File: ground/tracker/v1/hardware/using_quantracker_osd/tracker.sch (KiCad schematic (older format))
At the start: 20 parts, among them K1 CONN_3, K2 CONN_3, M1 OSD_v2_2, P1 CONN_2, SW1 SW_PUSH

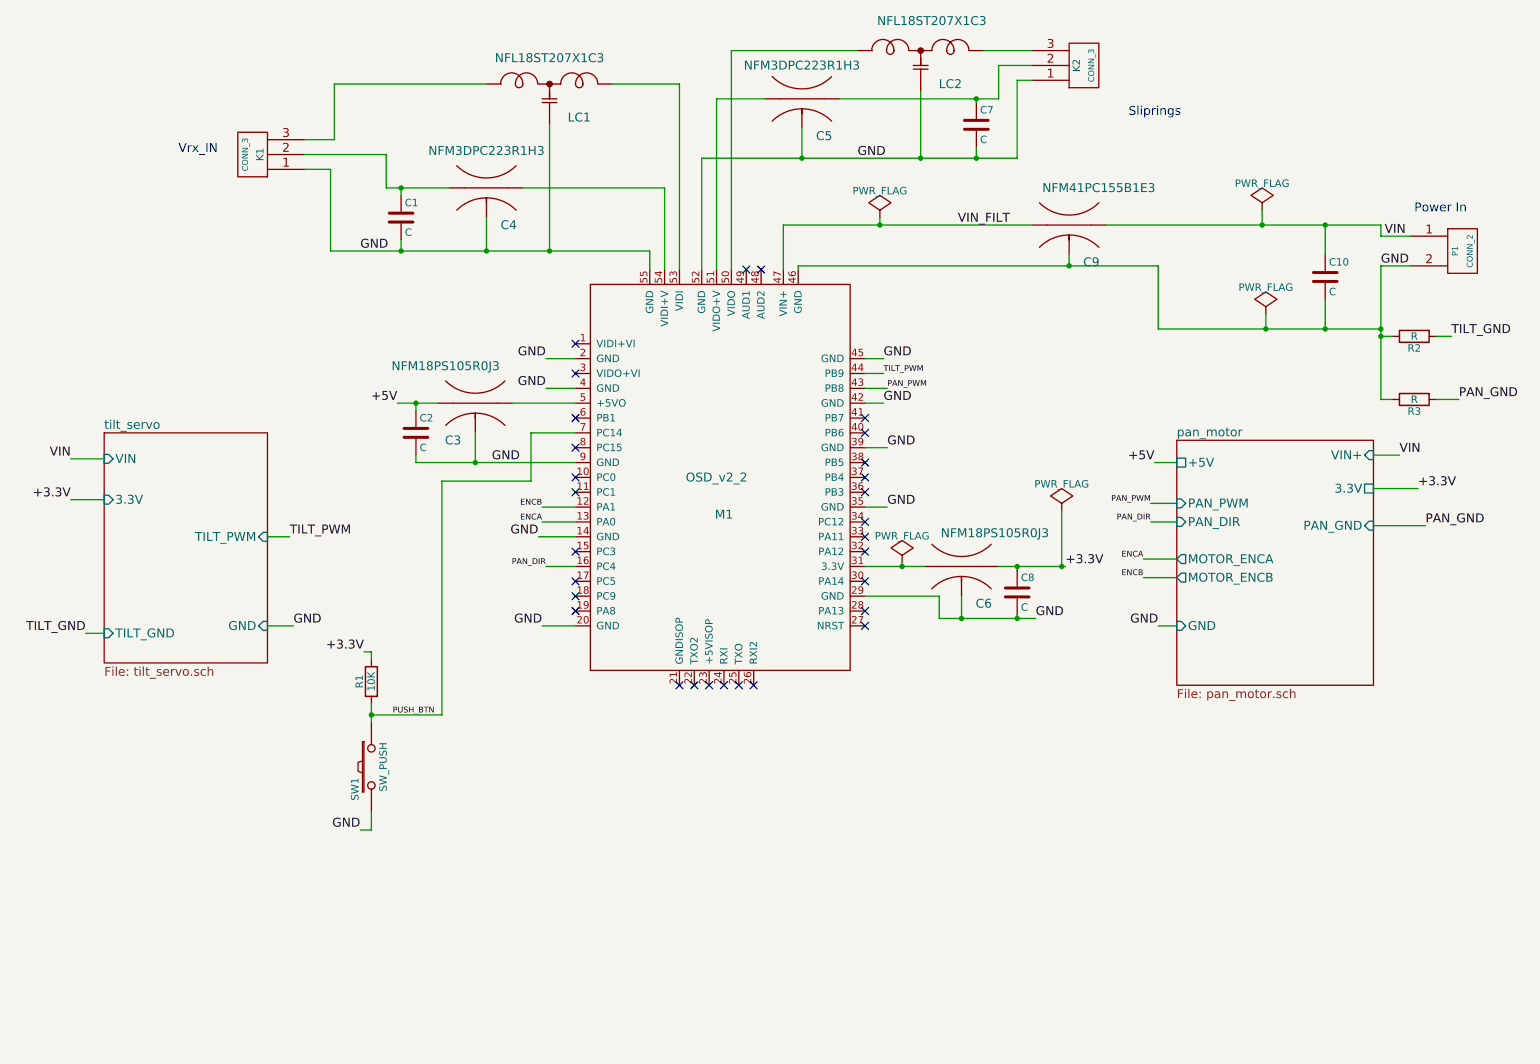
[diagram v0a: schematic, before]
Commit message: add i2c and gps connectors
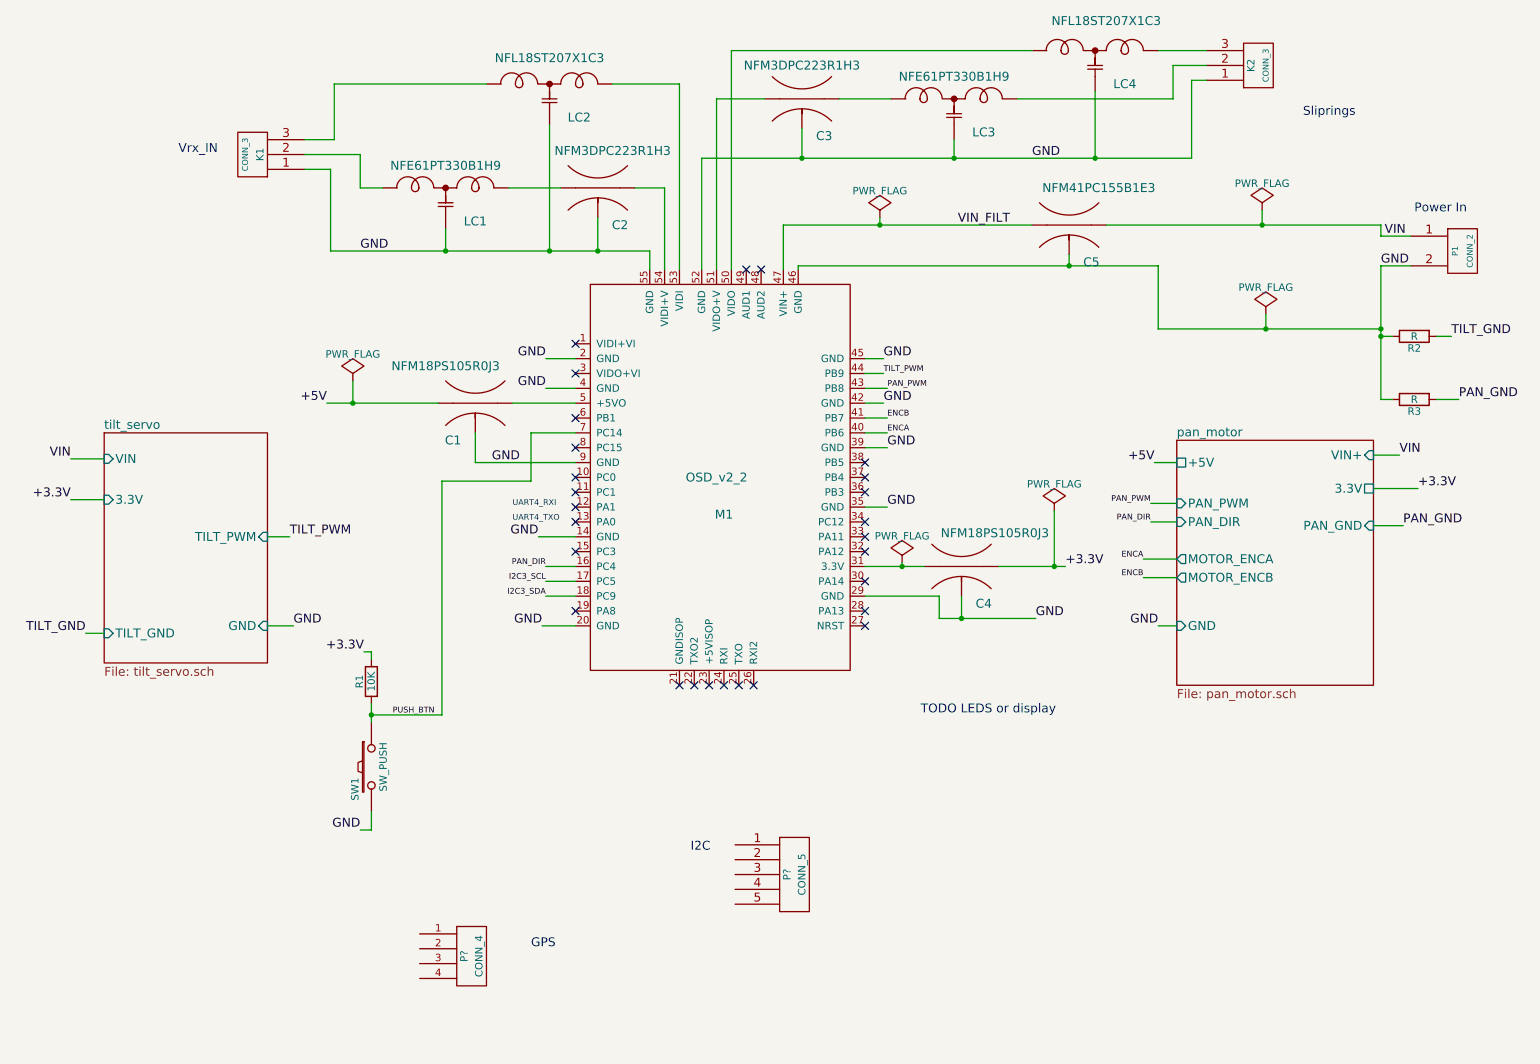
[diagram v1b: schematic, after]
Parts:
- removed C1, C10, C2, C7, C8: C, symbol C
- added LC1, LC3: NFE61PT330B1H9, symbol TLCFILT
- added P?: CONN_5, symbol CONN_5
- added P?: CONN_4, symbol CONN_4
- renumbered C3 to C1, C4 to C2, C5 to C3, C6 to C4, C9 to C5, LC1 to LC2, LC2 to LC4
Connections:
- net ENCA: now also M1.40 (PB6); no longer M1.13 (PA0)
- net ENCB: now also M1.41 (PB7); no longer M1.12 (PA1)
- net GND: now also LC1.2 (GND), LC3.2 (GND)
- net I2C3_SCL: now reaches M1.17 (PC5)
- net I2C3_SDA: now reaches M1.18 (PC9)
- net at K1.2 (PM): now also LC1.1 (Input); no longer C2.1 (IO1)
- net at K2.2 (PM): now also LC3.3 (Output); no longer C3.3 (IO2)
- new net: C2.1 (IO1), LC1.3 (Output)
- new net: C3.3 (IO2), LC3.1 (Input)
- no-connect marks 29 -> 27
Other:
- note added: "GPS"
- note added: "I2C"
- note added: "TODO LEDS or display"
- note added: "UART4_RXI"
- note added: "UART4_TXO"
- moved on the sheet: C2, K2, LC4

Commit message: move around some pin labels, preliminary still
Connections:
- net I2C3_SCL: now also M1.19 (PA8); no longer M1.17 (PC5)
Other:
- note added: "TIM11_CH1"
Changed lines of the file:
@@
 NoConn ~ 4700 3825
 NoConn ~ 4700 4225
-NoConn ~ 4700 4625
 NoConn ~ 5950 2325
 NoConn ~ 5850 2325
@@
 	1    0    0    -1
 $EndComp
-Text Label 4500 4425 2    39   ~ 0
+Text Label 4500 4625 2    39   ~ 0
 I2C3_SCL
 Text Label 4500 4525 2    39   ~ 0
 I2C3_SDA
-Wire Wire Line
-	4700 4425 4500 4425
 Wire Wire Line
 	4700 4525 4500 4525
@@
 Text Notes 5475 6250 0    60   ~ 0
 I2C
+Text Notes 6025 3050 0    39   ~ 0
+TIM11_CH1
+Wire Wire Line
+	4700 4625 4500 4625
+NoConn ~ 4700 4425
 $EndSCHEMATC

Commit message: still rearranging pinout
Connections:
- net PAN_PWM: now also M1.6 (PB1); no longer M1.43 (PB8)
- new net FrSky_PWM: M1.43 (PB8)
- no-connect marks 27 -> 26
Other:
- note added: "TIM10_CH1"
- note added: "TIM1_CH3N"
- note added: "TIM4_CH1"
- note added: "TIM4_CH2"
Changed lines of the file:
@@
 +3.3V
 Text Label 6800 3125 0    39   ~ 0
-PAN_PWM
+FrSky_PWM
 Wire Wire Line
 	6800 3125 6650 3125
@@
 NoConn ~ 6650 4625
 NoConn ~ 6650 4725
-NoConn ~ 4700 3325
 NoConn ~ 4700 3525
 NoConn ~ 4700 3725
@@
 	4700 4625 4500 4625
 NoConn ~ 4700 4425
+Text Notes 6025 3150 0    39   ~ 0
+TIM10_CH1
+Text Notes 6050 3450 0    39   ~ 0
+TIM4_CH1
+Text Notes 6075 3350 0    39   ~ 0
+TIM4_CH2
+Text Notes 5050 3350 0    39   ~ 0
+TIM1_CH3N
+Text Label 4550 3325 2    39   ~ 0
+PAN_PWM
+Wire Wire Line
+	4700 3325 4550 3325
 $EndSCHEMATC

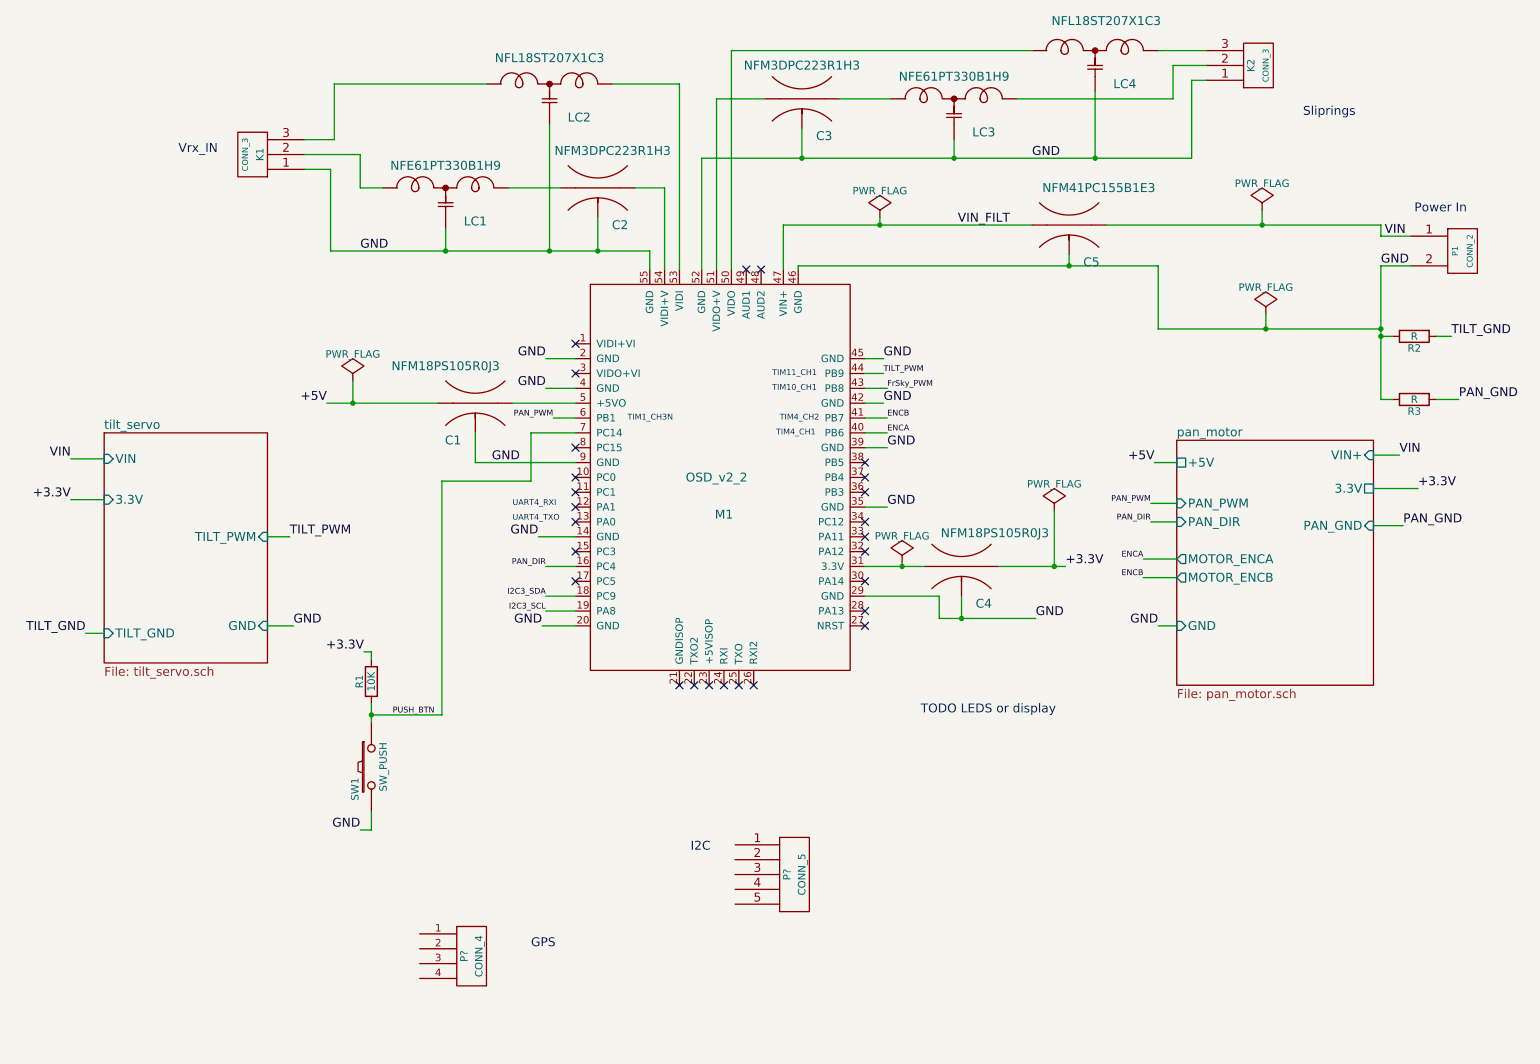
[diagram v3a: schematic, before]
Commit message: move encoder up out of pan motor schematic
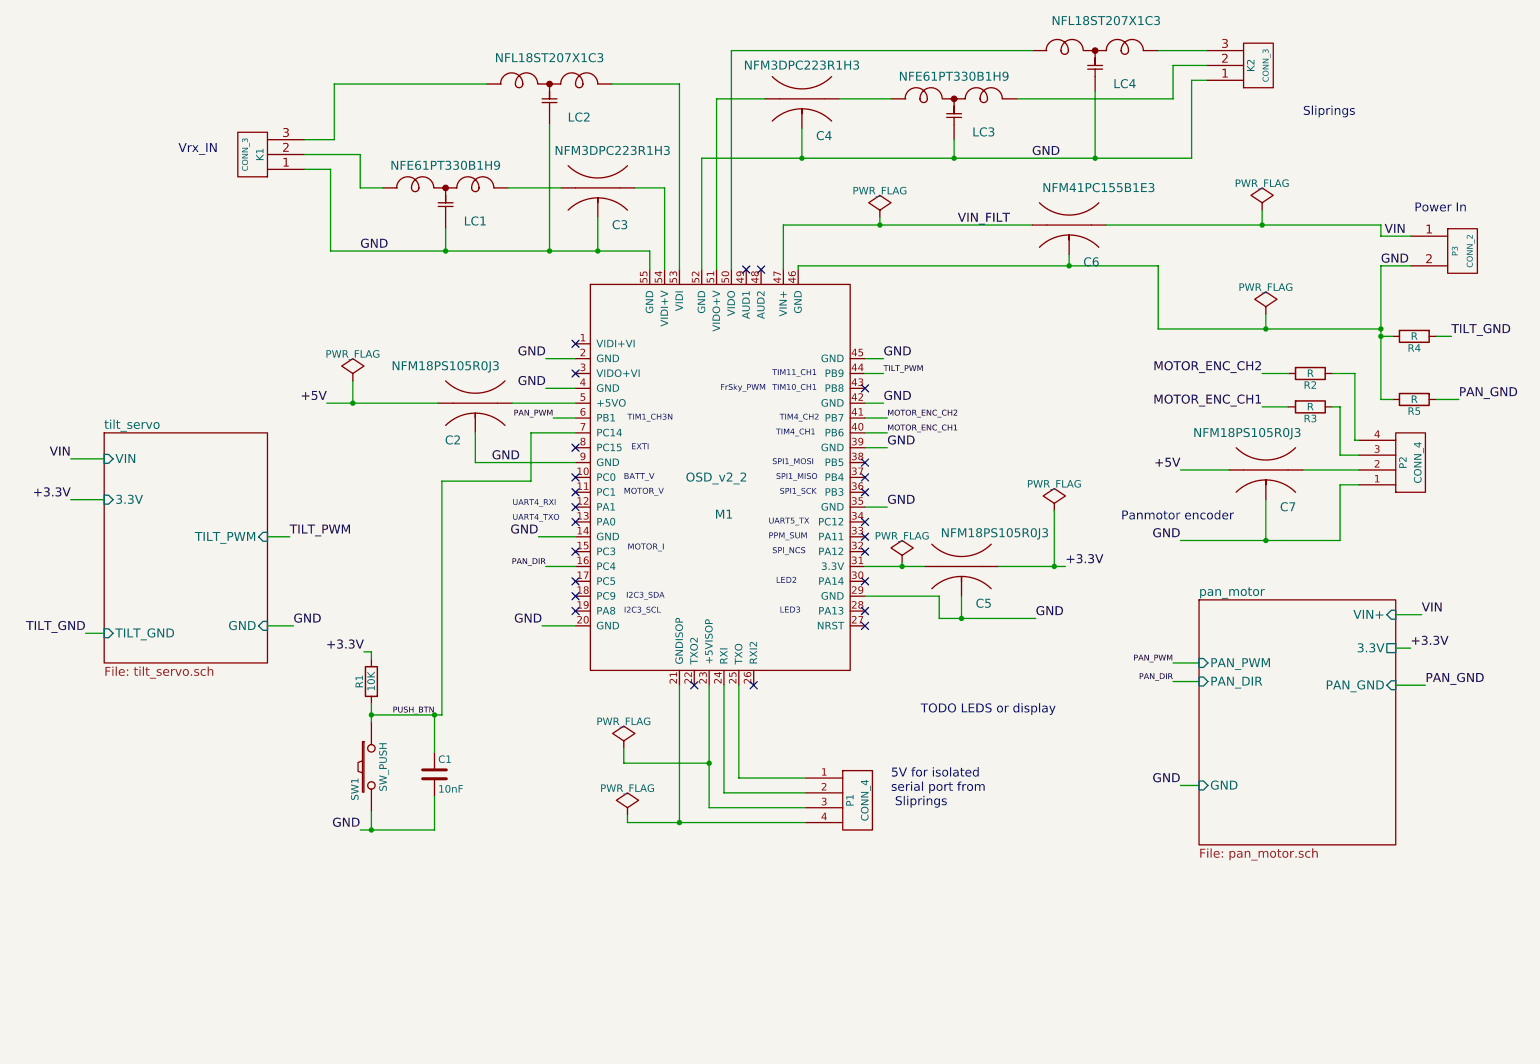
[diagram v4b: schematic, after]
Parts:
- removed P?: CONN_5, symbol CONN_5
- removed P?: CONN_4, symbol CONN_4
- added C1: 10nF, symbol C
- added C7: NFM18PS105R0J3, symbol CAP3T
- added P1, P2: CONN_4, symbol CONN_4
- added R2, R3: R, symbol R
- renumbered C1 to C2, C2 to C3, C3 to C4, C4 to C5, C5 to C6, P1 to P3, R2 to R4, R3 to R5
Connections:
- net +5V: now also C7.1 (IO1)
- net GND: now also C1.2, C7.2 (GND), P2.1 (P1)
- net PUSH_BTN: now also C1.1
- net at M1.21 (GNDISOP): now also P1.4 (P4)
- net at M1.23 (+5VISOP): now also P1.3 (P3)
- net at M1.24 (RXI): now also P1.2 (P2)
- net at M1.25 (TXO): now also P1.1 (P1)
- net ENCA renamed MOTOR_ENC_CH1
- net MOTOR_ENC_CH1: now also R3.2
- net ENCB renamed MOTOR_ENC_CH2
- net MOTOR_ENC_CH2: now also R2.2
- net FrSky_PWM: no longer names the net of M1.43 (PB8)
- net I2C3_SCL: no longer names the net of M1.19 (PA8)
- net I2C3_SDA: no longer names the net of M1.18 (PC9)
- new net: C7.3 (IO2), P2.2 (P2)
- new net: P2.3 (P3), R3.1
- new net: P2.4 (P4), R2.1
- no-connect marks 26 -> 25
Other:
- note added: "5V for isolated \nserial port from\n Sliprings"
- note added: "BATT_V"
- note added: "EXTI"
- note added: "FrSky_PWM"
- note added: "I2C3_SCL"
- note added: "I2C3_SDA"
- note added: "LED2"
- note added: "LED3"
- note added: "MOTOR_I"
- note added: "MOTOR_V"
- note added: "PPM_SUM"
- note added: "Panmotor encoder"
- note added: "SPI1_MISO"
- note added: "SPI1_MOSI"
- note added: "SPI1_SCK"
- note added: "SPI_NCS"
- note added: "UART5_TX"
- note removed: "GPS"
- note removed: "I2C"

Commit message: remove isolator frm pan motor
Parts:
- added C1: C, symbol C
- added C2, C3: CP1, symbol CP1
- added C5: NFM31PC276B0J3, symbol CAP3T
- added D1: D_Schottky, symbol D_Schottky
- added K2: CONN_3, symbol CONN_3
- added P4: CONN_5, symbol CONN_5
- added R4, R5, R6: R, symbol R
- renumbered C6 to C10, C7 to C11, C1 to C4, C2 to C6, C3 to C7, C4 to C8, C5 to C9, K2 to K3, R4 to R7, R5 to R8
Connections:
- net PAN_DIR: now also R5.2
- net PAN_GND: now also C1.2, C2.2, C3.2, C5.2 (GND), K2.1 (P1)
- net PAN_PWM: now also R4.2
- net ~NOT_PAN_DIR: now reaches M1.17 (PC5)
- net ~NOT_PAN_DIR: now also R6.2
- new net: P4.2, R6.1
- new net: P4.3, R5.1
- new net: P4.4, R4.1
- new net: C5.3 (IO2), K2.2 (PM)
- new net: C2.1, C3.1, C5.1 (IO1), D1.1 (K)
- new net VIN+: C1.1, D1.2 (A)
- no-connect marks 25 -> 27
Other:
- note added: "Pan Motor power"
- note added: "Pan motor control"

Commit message: tidy up tracker schematic a little
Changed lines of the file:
@@
 Vrx_IN
 Wire Wire Line
-	3050 2200 3825 2200
-Wire Wire Line
-	3825 2200 4525 2200
-Wire Wire Line
-	4525 2200 4850 2200
-Wire Wire Line
-	4850 2200 5200 2200
+	3050 2200 5200 2200
 Wire Wire Line
 	2875 1450 3075 1450
@@
 	5550 2325 5550 1575
 Wire Wire Line
-	5550 1575 6225 1575
-Wire Wire Line
-	6225 1575 7250 1575
-Wire Wire Line
-	7250 1575 8200 1575
-Wire Wire Line
-	8200 1575 8850 1575
+	5550 1575 8850 1575
 Wire Wire Line
 	8850 1575 8850 1050
@@
 	6100 2325 6100 2025
 Wire Wire Line
-	6100 2025 6750 2025
-Wire Wire Line
-	6750 2025 7775 2025
+	6100 2025 7775 2025
 $Comp
 L CONN_2 P3
@@
 Connection ~ 8025 2300
 Wire Wire Line
-	8275 2025 9325 2025
-Wire Wire Line
-	9325 2025 10125 2025
+	8275 2025 10125 2025
 Wire Wire Line
 	10125 2100 10325 2100
@@
 $EndComp
 Wire Wire Line
-	8625 2725 9350 2725
-Wire Wire Line
-	9350 2725 10125 2725
+	8625 2725 10125 2725
 Wire Wire Line
 	10500 2775 10600 2775
@@
 	10500 3200 10650 3200
 Wire Wire Line
-	6650 4325 6900 4325
-Wire Wire Line
-	6900 4325 7050 4325
+	6650 4325 7050 4325
 $Comp
 L TLCFILT LC2
@@
 F0 "tilt_servo" 60
 F1 "tilt_servo.sch" 60
-F4 "VIN" I L 1525 3600 60
-F5 "TILT_GND" I L 1525 4775 60
-F6 "TILT_PWM" I R 2625 4125 60
+F2 "VIN" I L 1525 3600 60
+F3 "TILT_GND" I L 1525 4775 60
+F4 "TILT_PWM" I R 2625 4125 60
 $EndSheet
 Wire Wire Line
@@
 $EndComp
 Wire Wire Line
-	3025 3225 3200 3225
-Wire Wire Line
-	3200 3225 3775 3225
+	3025 3225 3775 3225
 $Comp
 L CAP3T C9
@@
 $EndComp
 Wire Wire Line
-	7550 4325 7925 4325
-Wire Wire Line
-	7925 4325 8000 4325
+	7550 4325 8000 4325
 Wire Wire Line
 	1525 3600 1300 3600
@@
 	7150 4525 7150 4675
 Wire Wire Line
-	7150 4675 7300 4675
-Wire Wire Line
-	7300 4675 7800 4675
+	7150 4675 7800 4675
 Wire Wire Line
 	7300 4675 7300 4525
@@
 Connection ~ 7300 4675
 Wire Wire Line
-	6200 2300 8025 2300
-Wire Wire Line
-	8025 2300 8625 2300
-Wire Wire Line
-	10125 2300 10125 2725
-Wire Wire Line
-	10125 2725 10125 2775
-Wire Wire Line
-	10125 2775 10125 3200
+	6200 2300 8625 2300
+Wire Wire Line
+	10125 2300 10125 3200
 Wire Wire Line
 	10125 2300 10325 2300
@@
 GND
 Wire Wire Line
-	3250 6100 3325 6100
-Wire Wire Line
-	3325 6100 3750 6100
+	3250 6100 3750 6100
 Wire Wire Line
 	3325 6100 3325 5975
@@
 	3325 4900 3325 4950
 Wire Wire Line
-	3325 5250 3325 5325
-Wire Wire Line
-	3325 5325 3325 5375
-Wire Wire Line
-	3325 5325 3750 5325
-Wire Wire Line
-	3750 5325 3800 5325
+	3325 5250 3325 5375
+Wire Wire Line
+	3325 5325 3800 5325
 Connection ~ 3325 5325
 Text Label 3750 5325 2    39   ~ 0
@@
 	5400 5125 5400 6050
 Wire Wire Line
-	5050 6050 5400 6050
-Wire Wire Line
-	5400 6050 6250 6050
+	5050 6050 6250 6050
 Wire Wire Line
 	5700 5125 5700 5850
@@
 	5700 5850 6250 5850
 Wire Wire Line
-	5600 5125 5600 5650
-Wire Wire Line
-	5600 5650 5600 5950
+	5600 5125 5600 5950
 Wire Wire Line
 	5600 5950 6250 5950
@@
 Panmotor encoder
 Wire Wire Line
-	8775 4150 9350 4150
-Wire Wire Line
-	9350 4150 9850 4150
+	8775 4150 9850 4150
 Wire Wire Line
 	9975 3775 9850 3775
@@
 $EndComp
 Wire Wire Line
-	1975 7550 2250 7550
-Wire Wire Line
-	2250 7550 2925 7550
-Wire Wire Line
-	2925 7550 3225 7550
-Wire Wire Line
-	3225 7550 3750 7550
-Wire Wire Line
-	3750 7550 4600 7550
+	1975 7550 4600 7550
 $Comp
 L D_Schottky D1
@@
 $EndComp
 Wire Wire Line
-	1800 6650 2250 6650
-Wire Wire Line
-	2250 6650 2475 6650
-Wire Wire Line
-	2775 6650 2925 6650
-Wire Wire Line
-	2925 6650 3225 6650
-Wire Wire Line
-	3225 6650 3500 6650
+	1800 6650 2475 6650
+Wire Wire Line
+	2775 6650 3500 6650
 Wire Wire Line
 	4000 6650 4325 6650
